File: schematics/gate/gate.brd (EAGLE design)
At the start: 87.3 x 50.8 mm, 19 parts, among them IC1 7805L, IC3 LM1117T-1.8, Q1 BC548, Q2 BC548

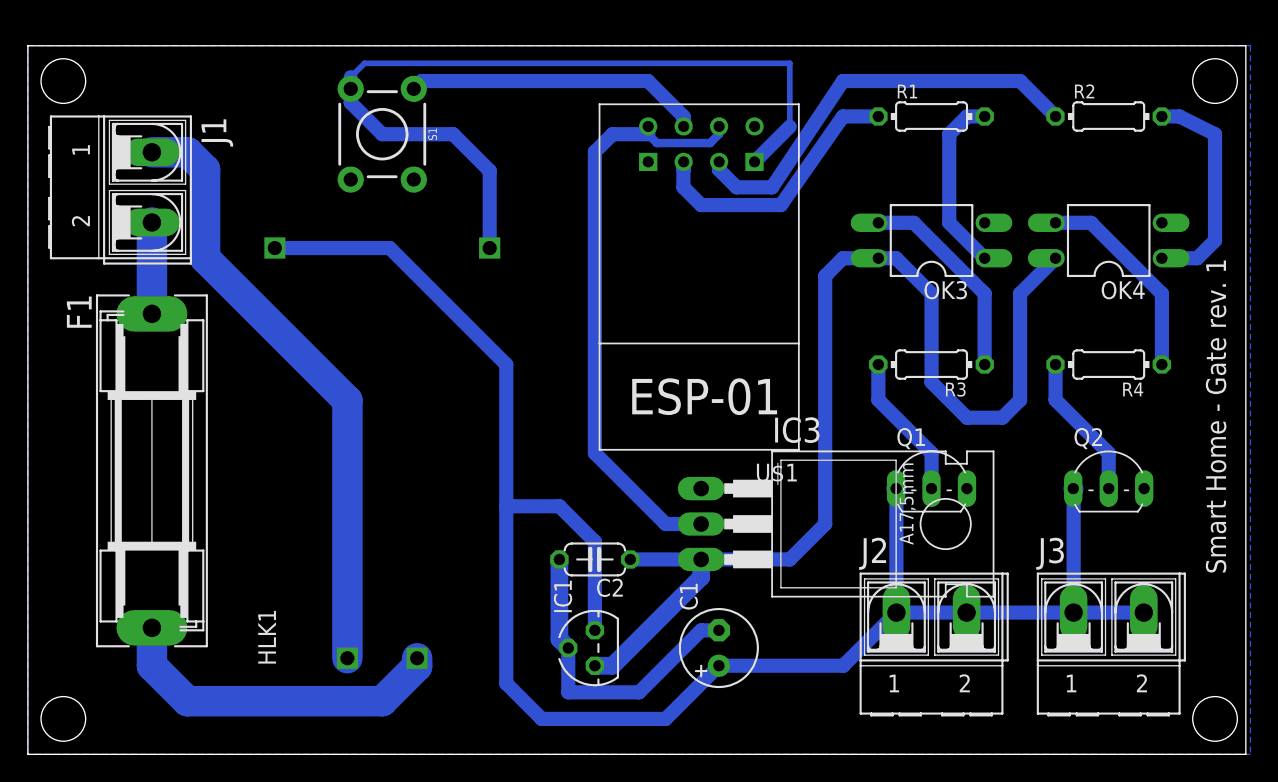
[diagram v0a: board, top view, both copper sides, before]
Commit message: change package 7805 and change ground plane
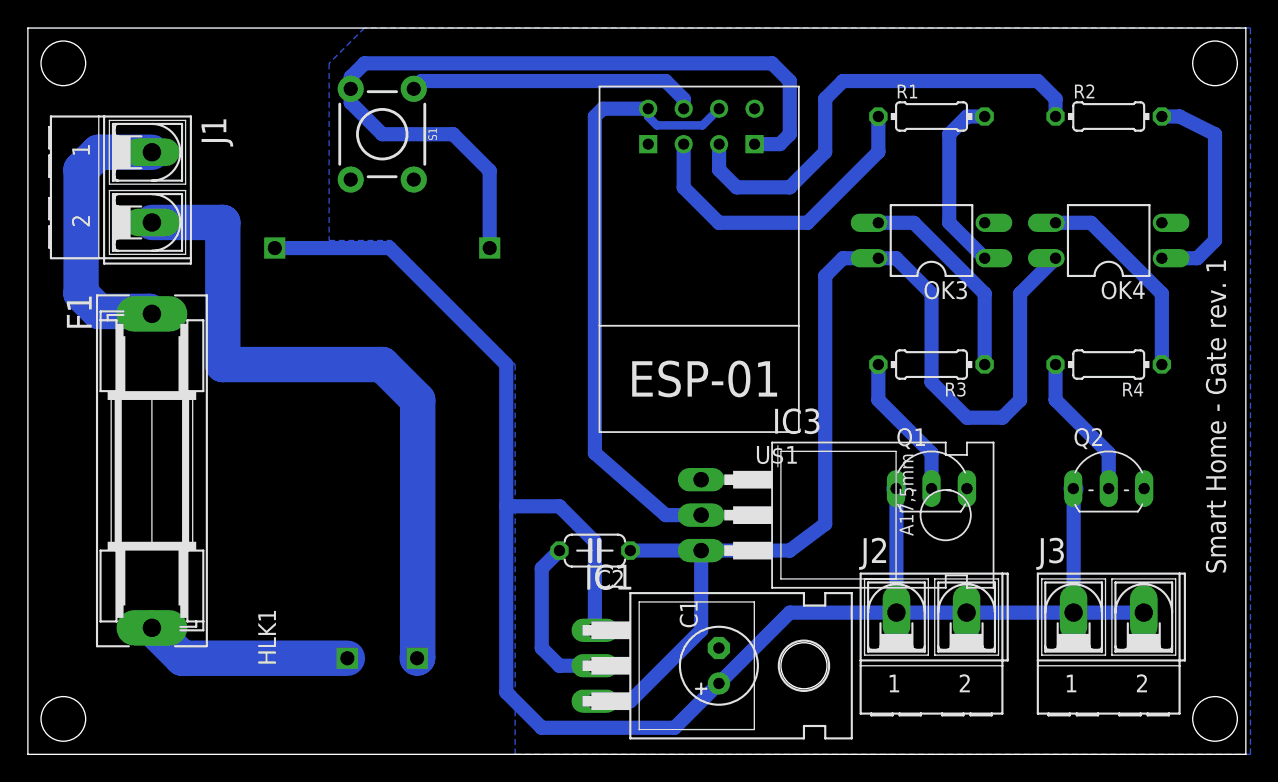
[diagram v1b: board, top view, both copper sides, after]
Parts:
- IC1: value 7805L -> 7805T; device linear:TO92 -> linear:TO220H
- moved IC1 10.2 mm to (50.8, 6.35), turned to 270 degrees
- moved U$1 1.27 mm to (48.3, 38.1)
- moved C1 1.27 mm to (49.5, 6.35)
- moved C2 0.63 mm to (40.6, 14.6)
- moved IC3 0.63 mm to (54.6, 17.1)
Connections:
- net 12V: now also IC1.1; no longer IC1.3
- net 5V: now also IC1.3; no longer IC1.1
- net N$1: now also F1.1; no longer HLK1.P$1
- net N$2: now also F1.2, HLK1.P$1; no longer F1.1, J1.2
- net N$3: now also J1.2; no longer F1.2
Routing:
- net N$3: track 24.4 -> 48.8 mm
- net N$1: track 43.6 -> 20.2 mm
- net GND: track 81.8 -> 70.2 mm
- net N$2: track 6.55 -> 14.9 mm
- net 5V: track 79.0 -> 82.5 mm
- net N$12: track 30.3 -> 33.7 mm
- net N$13: track 19.6 -> 22.8 mm
- net N$14: track 42.9 -> 43.9 mm
- net 12V: track 124.4 -> 125.3 mm
- net N$10: track 21.3 -> 20.8 mm
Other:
- board size 87.3 x 50.8 mm -> 87.3 x 52.1 mm
